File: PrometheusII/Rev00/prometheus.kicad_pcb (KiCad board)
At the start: 4 copper layers, 153.2 x 128.5 mm, 190 parts, among them J1 0878311420, J2 Conn_02x08_Odd_Even, J3 Conn_02x05_Odd_Even, J4 Conn_02x05_Odd_Even, J5 Conn_02x04_Odd_Even, J6 Conn_02x04_Odd_Even, J8 Conn_02x03_Odd_Even, J9 Conn_02x03_Odd_Even, Q1 MMBF4391, Q2 MMBF4391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

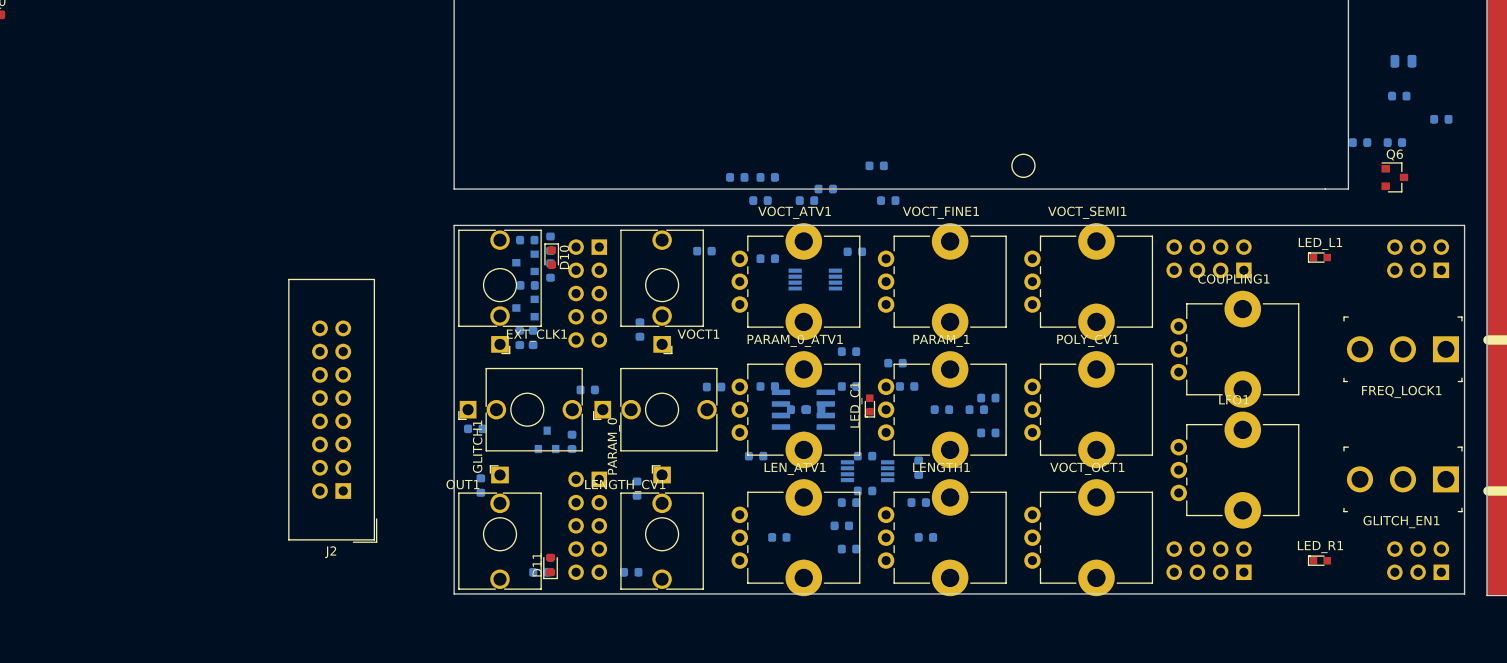
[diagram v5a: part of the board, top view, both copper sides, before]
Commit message: Placed lfo indicator circuitry
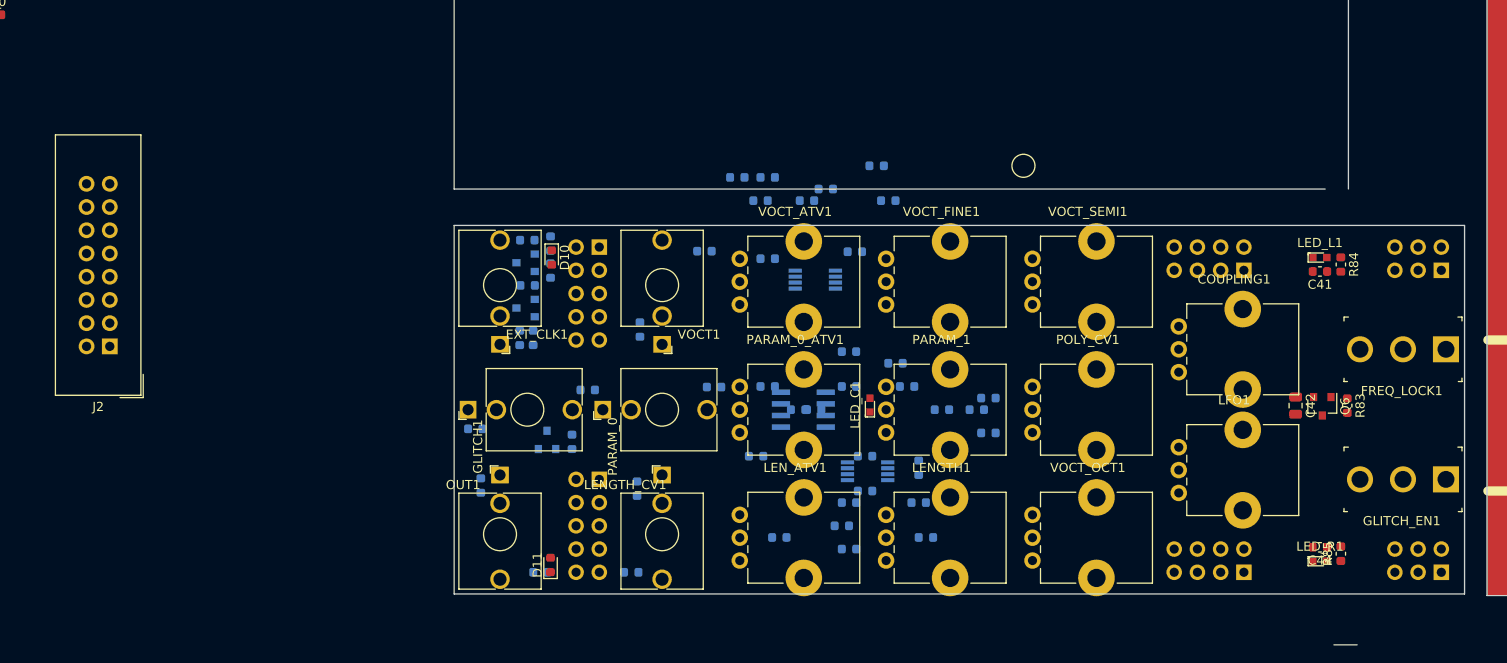
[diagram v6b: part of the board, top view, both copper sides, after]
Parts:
- added C44: 1u, Capacitor_SMD:C_0603_1608Metric, F.Cu at (111.2, 124.3)
- C41, C42, R83, R84, R85: moved to F.Cu
- moved R85 50.4 mm to (113.5, 125.0), turned to 90 degrees
- moved C42 39.5 mm to (108.5, 108.8), turned to 270 degrees
- moved J2 30.0 mm to (-21.1, 102.3)
- moved R83 28.8 mm to (114.2, 108.8), turned to 270 degrees
- moved Q6 26.2 mm to (111.4, 108.8), turned to 270 degrees
- moved R84 19.3 mm to (113.5, 93.3), turned to 270 degrees
- moved C41 16.3 mm to (111.2, 94.1), turned to 180 degrees
- moved LED_R1 0.08 mm to (111.2, 125.8)
- moved LED_L1 0.05 mm to (111.2, 92.6)
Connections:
- J8 pad 6: Net-(J8-Pad6) -> /LFO_LED_T
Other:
- board size 153.2 x 128.5 mm -> 153.2 x 133.9 mm

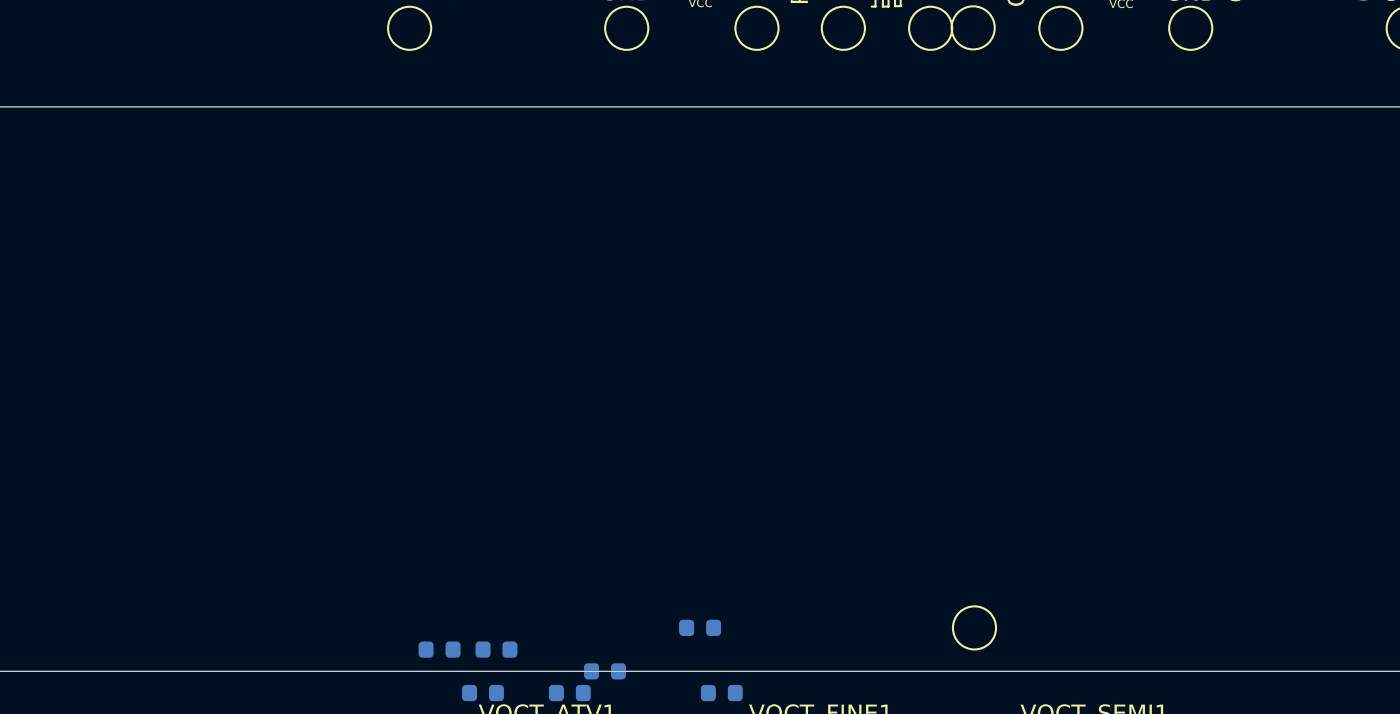
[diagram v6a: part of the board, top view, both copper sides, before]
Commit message: Split signal nets across boards
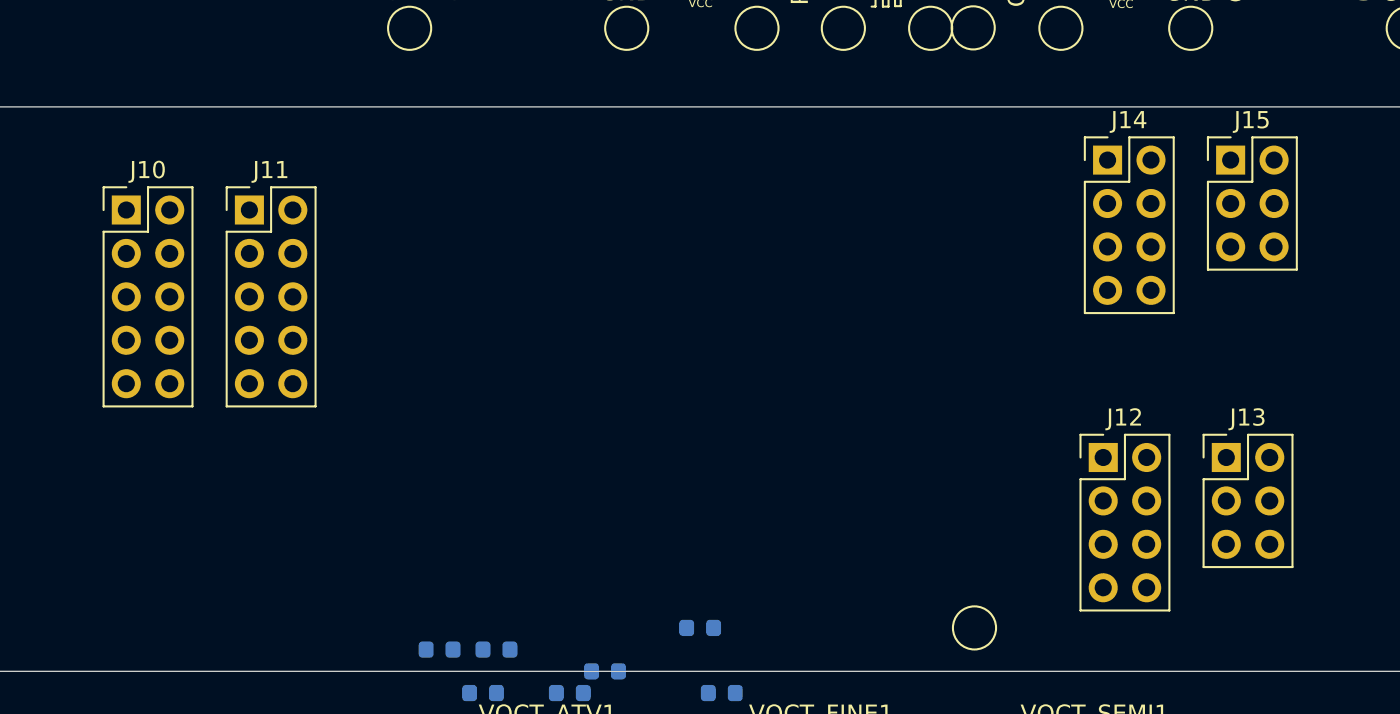
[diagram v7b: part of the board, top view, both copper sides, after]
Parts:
- added J10: Conn_02x05_Odd_Even, Connector_PinHeader_2.54mm:PinHeader_2x05_P2.54mm_Vertical, F.Cu at (29.1, 58.1)
- added J11: Conn_02x05_Odd_Even, Connector_PinHeader_2.54mm:PinHeader_2x05_P2.54mm_Vertical, F.Cu at (36.3, 58.1)
- added J12: Conn_02x04_Odd_Even, Connector_PinHeader_2.54mm:PinHeader_2x04_P2.54mm_Vertical, F.Cu at (86.3, 72.6)
- added J13: Conn_02x03_Odd_Even, Connector_PinHeader_2.54mm:PinHeader_2x03_P2.54mm_Vertical, F.Cu at (93.5, 72.6)
- added J14: Conn_02x04_Odd_Even, Connector_PinHeader_2.54mm:PinHeader_2x04_P2.54mm_Vertical, F.Cu at (86.6, 55.2)
- added J15: Conn_02x03_Odd_Even, Connector_PinHeader_2.54mm:PinHeader_2x03_P2.54mm_Vertical, F.Cu at (93.8, 55.2)
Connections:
- net /PARAM_0 renamed /PARAM_0_P
- COUPLING1 pad 2: /CV_FILT -> /CV_FILT_P
- FREQ_LOCK1 pad 2: /FREQ_LOCK_T -> /FREQ_LOCK_P
- GLITCH_EN1 pad 2: /GLITCH_EN_T -> /GLITCH_EN_P
- J3 pad 2: /EXT_CLK -> /EXT_CLK_P
- J3 pad 3: /VOCT_ATV -> /VOCT_ATV_P
- J3 pad 5: /VOCT_CV -> /VOCT_CV_P
- J3 pad 8: /EXT_CLK_EN_T -> /EXT_CLK_EN_P
- J4 pad 10: /OUT -> /OUT_P
- J4 pad 4: /GLITCH_IN_T -> /GLITCH_IN_P
- J4 pad 7: /LEN_CV -> /LEN_CV_P
- J6 pad 2: Net-(J6-Pad2) -> /POLY_P
- J6 pad 4: Net-(J6-Pad4) -> /TAPS_LED_P
- J6 pad 6: Net-(J6-Pad6) -> /VOCT_OCT_P
- J6 pad 8: Net-(J6-Pad8) -> /LEN_KNOB_P
- J8 pad 2: Net-(J8-Pad2) -> /GLITCH_EN_P
- J8 pad 4: Net-(J8-Pad4) -> /LFO_LED_P
- J8 pad 6: /LFO_LED_T -> /LFO_P
- LENGTH1 pad 2: /LEN_KNOB -> /LEN_KNOB_P
- LFO1 pad 2: /LFO -> /LFO_P
- PARAM_1 pad 2: /PARAM_1 -> /PARAM_1_P
- POLY_CV1 pad 2: /POLY -> /POLY_P
- Q3 pad 3: /GLITCH_IN_T -> /GLITCH_IN_P
- Q4 pad 3: /EXT_CLK_EN_T -> /EXT_CLK_EN_P
- R51 pad 1: /OUT -> /OUT_P
- R52 pad 1: /GLITCH_IN_T -> /GLITCH_IN_P
- R56 pad 1: /FREQ_LOCK_T -> /FREQ_LOCK_P
- R59 pad 1: /GLITCH_EN_T -> /GLITCH_EN_P
- R61 pad 1: /EXT_CLK_EN_T -> /EXT_CLK_EN_P
- R63 pad 1: /VOCT_CV -> /VOCT_CV_P
- R66 pad 1: /VOCT_CV -> /VOCT_CV_P
- R68 pad 1: /EXT_CLK -> /EXT_CLK_P
- R69 pad 1: /EXT_CLK -> /EXT_CLK_P
- R78 pad 1: /LEN_CV -> /LEN_CV_P
- R79 pad 1: /PARAM_0_CV -> /PARAM_0_CV_P
- R81 pad 1: /LEN_CV -> /LEN_CV_P
- R82 pad 1: /PARAM_0_CV -> /PARAM_0_CV_P
- R83 pad 2: /LFO_LED_T -> /LFO_LED_P
- R86 pad 2: /TAPS_LED_T -> /TAPS_LED_P
- VOCT_ATV1 pad 2: /VOCT_ATV -> /VOCT_ATV_P
- VOCT_FINE1 pad 2: /VOCT_FINE -> /VOCT_FINE_P
- VOCT_OCT1 pad 2: /VOCT_OCT -> /VOCT_OCT_P
- VOCT_SEMI1 pad 2: /VOCT_SEMI -> /VOCT_SEMI_P

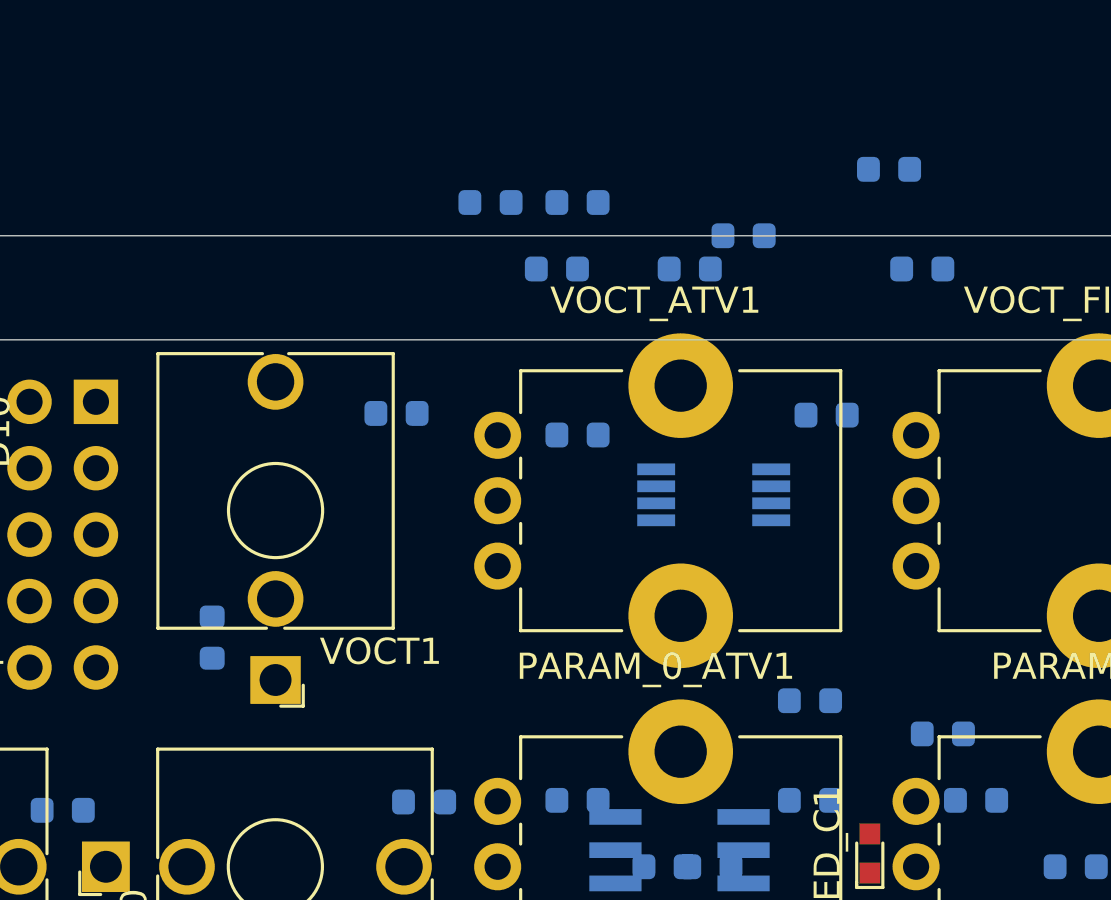
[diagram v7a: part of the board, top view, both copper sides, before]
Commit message: Placed voct buffer
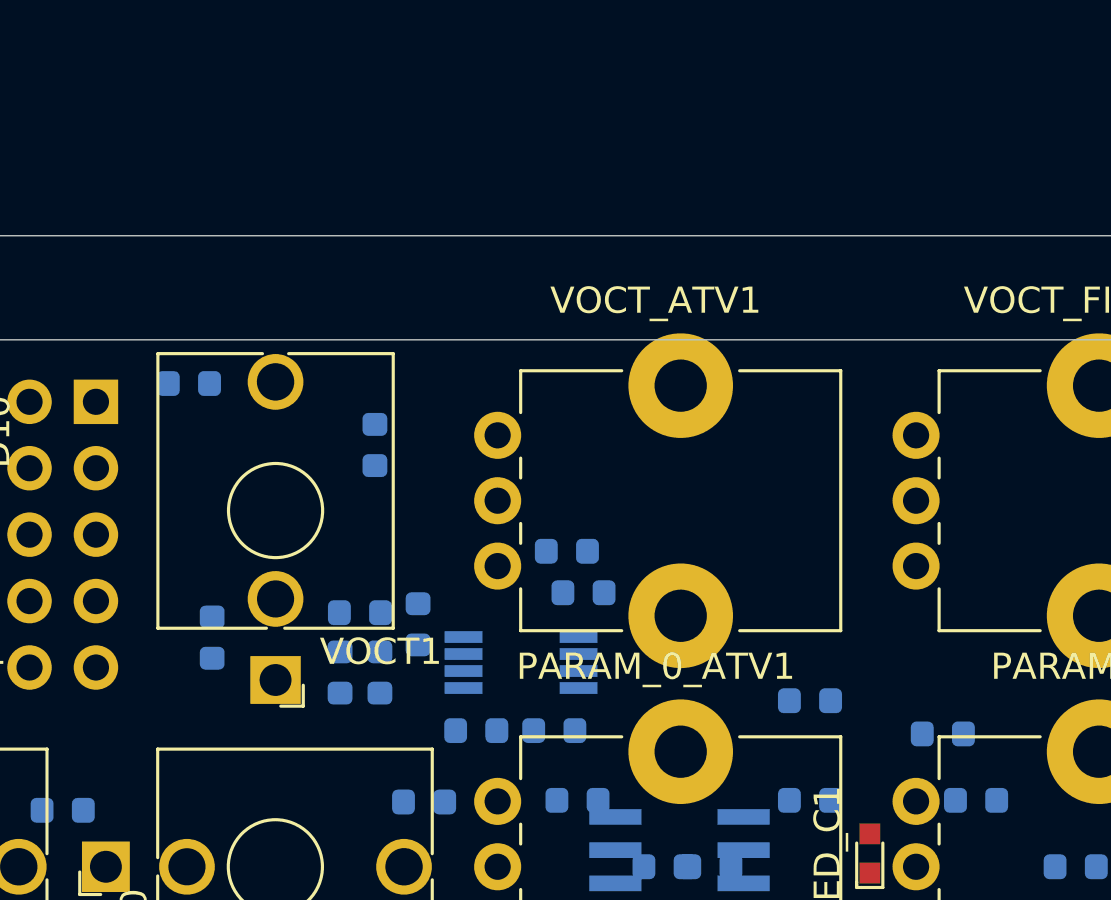
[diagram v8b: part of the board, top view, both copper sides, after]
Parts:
- moved R66 28.5 mm to (41.7, 101.8), turned to 270 degrees
- moved R57 22.0 mm to (43.1, 93.1), turned to 90 degrees
- moved C35 21.7 mm to (43.2, 101.8), turned to 270 degrees
- moved R53 19.5 mm to (46.9, 104.0), turned to 180 degrees
- moved R63 19.4 mm to (42.5, 99.5), turned to 0 degrees
- moved C37 17.7 mm to (49.9, 104.0)
- moved R58 16.4 mm to (44.7, 99.9), turned to 270 degrees
- moved R80 14.9 mm to (51.0, 98.7)
- moved U9 9.77 mm to (48.6, 101.4), turned to 0 degrees
- moved D4 8.02 mm to (35.9, 90.7), turned to 180 degrees
- moved R77 4.46 mm to (50.4, 97.2)
